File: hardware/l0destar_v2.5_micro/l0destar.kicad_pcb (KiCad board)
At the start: 4 copper layers, 65.4 x 34.4 mm, 74 parts

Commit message: tweaked layouts
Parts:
- removed S1R3: 100K, Resistor_SMD:R_0402_1005Metric
- S2D2, S2D4: value PTVS30VS1UTR,115 -> PTVS33VS1UTR,115
- renumbered C2 to S1C1, C3 to S1C2, S6C6 to S6C1, S6C7 to S6C2, S6C8 to S6C3, S6C9 to S6C4, S6C10 to S6C5, S6L2 to S6L1, S6R4 to S6R1, S6R5 to S6R2, S6R6 to S6R3, S6U2 to S6U1, S6U3 to S6U2, S7Q3 to S7Q1, S7Q4 to S7Q2, S7R5 to S7R1, S7R6 to S7R2, S7R7 to S7R3, S7R8 to S7R4
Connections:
- S1J2 pad 2: VSYS -> unconnected-(S1J2-VSYS-Pad2)
- S1J2 pad 4: Net-(S1J2-ENABLE) -> unconnected-(S1J2-ENABLE-Pad4)
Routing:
- net VSYS: track 3.45 -> 0.00 mm
- net Net-(S1J2-ENABLE): track 3.13 -> 0.00 mm
- net GND: track 75.0 -> 74.7 mm, vias 125 -> 103
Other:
- board text removed: "ENABLE"
- board text removed: "VSYS"

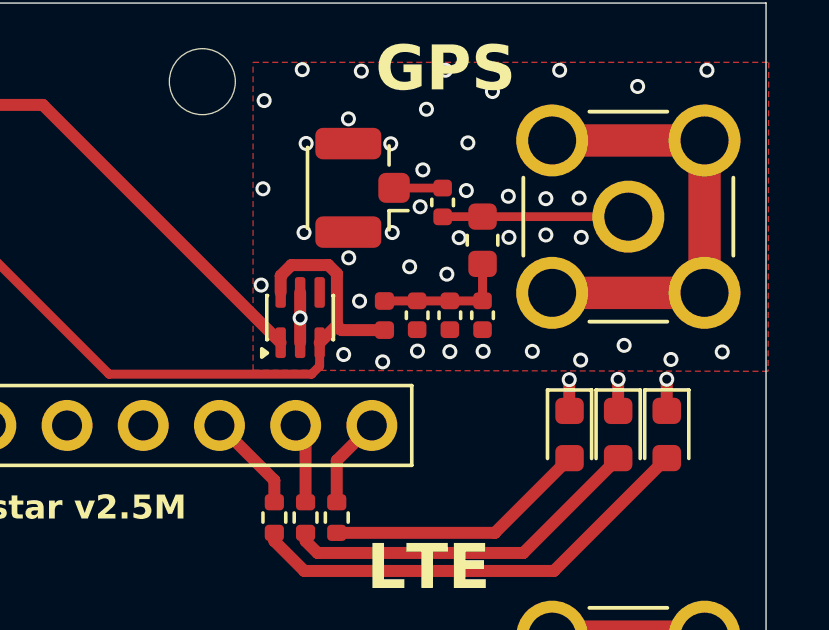
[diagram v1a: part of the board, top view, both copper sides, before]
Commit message: fix bias tee cap ordering on all boards
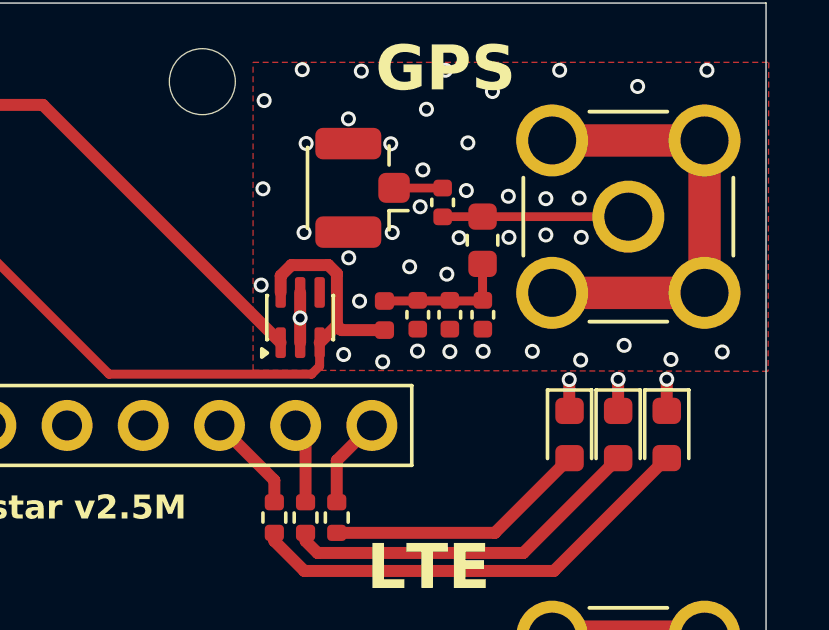
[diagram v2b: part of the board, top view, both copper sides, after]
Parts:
- moved S15C4 2.16 mm to (77.6, 85.0)
- moved S15C2 1.10 mm to (79.8, 85.0)
- moved S15C3 1.09 mm to (78.7, 85.0)
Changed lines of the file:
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@@
 	(footprint "Capacitor_SMD:C_0402_1005Metric"
 		(layer "F.Cu")
-		(at 77.61 84.97625 -90)
+		(at 78.7 84.96 -90)
 		(descr "Capacitor SMD 0402 (1005 Metric), square (rectangular) end terminal, IPC-7351 nominal, (Body size source: IPC-SM-782 page 76, https://www.pcb-3d.com/wordpress/wp-content/uploads/ipc-sm-782a_amendment_1_and_2.pdf)")
 		(tags "capacitor")
@@
 	(footprint "Capacitor_SMD:C_0402_1005Metric"
 		(layer "F.Cu")
-		(at 78.7 84.97625 -90)
+		(at 79.8 84.96 -90)
 		(descr "Capacitor SMD 0402 (1005 Metric), square (rectangular) end terminal, IPC-7351 nominal, (Body size source: IPC-SM-782 page 76, https://www.pcb-3d.com/wordpress/wp-content/uploads/ipc-sm-782a_amendment_1_and_2.pdf)")
 		(tags "capacitor")
@@
 	(footprint "Capacitor_SMD:C_0402_1005Metric"
 		(layer "F.Cu")
-		(at 79.79 84.97625 -90)
+		(at 77.63 84.96 -90)
 		(descr "Capacitor SMD 0402 (1005 Metric), square (rectangular) end terminal, IPC-7351 nominal, (Body size source: IPC-SM-782 page 76, https://www.pcb-3d.com/wordpress/wp-content/uploads/ipc-sm-782a_amendment_1_and_2.pdf)")
 		(tags "capacitor")
